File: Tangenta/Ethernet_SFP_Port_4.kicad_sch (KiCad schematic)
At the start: 17 parts, among them J25 HC-SFP-01L

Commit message: Fixes, before checks.
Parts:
- C166, C167, C168, C169: symbol C_Small:C_Small -> Device:C_Small
- J25: symbol HC-SFP-01L:HC-SFP-01L -> SFP_CAGE:HC-SFP-01L
- R141, R142, R143, R144, R145, R146, R147, R148, R149, R150, R151: symbol R_Small_US:R_Small_US -> Device:R_Small_US
- S1: symbol HC-SFP-20P:HC-SFP-20P -> SFP_Connector:HC-SFP-20P
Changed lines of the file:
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@@
 	)
 	(symbol
-		(lib_id "C_Small:C_Small")
+		(lib_id "Device:C_Small")
 		(at 66.04 64.77 270)
 		(unit 1)
@@
 	)
 	(symbol
-		(lib_id "R_Small_US:R_Small_US")
+		(lib_id "Device:R_Small_US")
 		(at 224.79 128.905 180)
 		(unit 1)
@@
 	)
 	(symbol
-		(lib_id "R_Small_US:R_Small_US")
+		(lib_id "Device:R_Small_US")
 		(at 139.7 118.11 90)
 		(unit 1)
@@
 	)
 	(symbol
-		(lib_id "HC-SFP-01L:HC-SFP-01L")
+		(lib_id "SFP_CAGE:HC-SFP-01L")
 		(at 159.385 76.835 0)
 		(unit 1)
@@
 	)
 	(symbol
-		(lib_id "R_Small_US:R_Small_US")
+		(lib_id "Device:R_Small_US")
 		(at 217.17 140.335 180)
 		(unit 1)
@@
 	)
 	(symbol
-		(lib_id "R_Small_US:R_Small_US")
+		(lib_id "Device:R_Small_US")
 		(at 139.7 133.35 90)
 		(unit 1)
@@
 	)
 	(symbol
-		(lib_id "C_Small:C_Small")
+		(lib_id "Device:C_Small")
 		(at 78.74 59.69 270)
 		(unit 1)
@@
 	)
 	(symbol
-		(lib_id "HC-SFP-20P:HC-SFP-20P")
+		(lib_id "SFP_Connector:HC-SFP-20P")
 		(at 159.385 127 0)
 		(unit 1)
@@
 	)
 	(symbol
-		(lib_id "R_Small_US:R_Small_US")
+		(lib_id "Device:R_Small_US")
 		(at 217.17 128.905 180)
 		(unit 1)
@@
 	)
 	(symbol
-		(lib_id "R_Small_US:R_Small_US")
+		(lib_id "Device:R_Small_US")
 		(at 198.755 113.03 180)
 		(unit 1)
@@
 	)
 	(symbol
-		(lib_id "C_Small:C_Small")
+		(lib_id "Device:C_Small")
 		(at 78.74 67.31 270)
 		(unit 1)
@@
 	)
 	(symbol
-		(lib_id "R_Small_US:R_Small_US")
+		(lib_id "Device:R_Small_US")
 		(at 224.79 140.335 180)
 		(unit 1)
@@
 	)
 	(symbol
-		(lib_id "C_Small:C_Small")
+		(lib_id "Device:C_Small")
 		(at 66.04 57.15 270)
 		(unit 1)
@@
 	)
 	(symbol
-		(lib_id "R_Small_US:R_Small_US")
+		(lib_id "Device:R_Small_US")
 		(at 198.755 125.095 180)
 		(unit 1)
@@
 	)
 	(symbol
-		(lib_id "R_Small_US:R_Small_US")
+		(lib_id "Device:R_Small_US")
 		(at 206.375 113.03 180)
 		(unit 1)
@@
 	)
 	(symbol
-		(lib_id "R_Small_US:R_Small_US")
+		(lib_id "Device:R_Small_US")
 		(at 139.7 128.27 90)
 		(unit 1)
@@
 	)
 	(symbol
-		(lib_id "R_Small_US:R_Small_US")
+		(lib_id "Device:R_Small_US")
 		(at 206.375 125.095 180)
 		(unit 1)

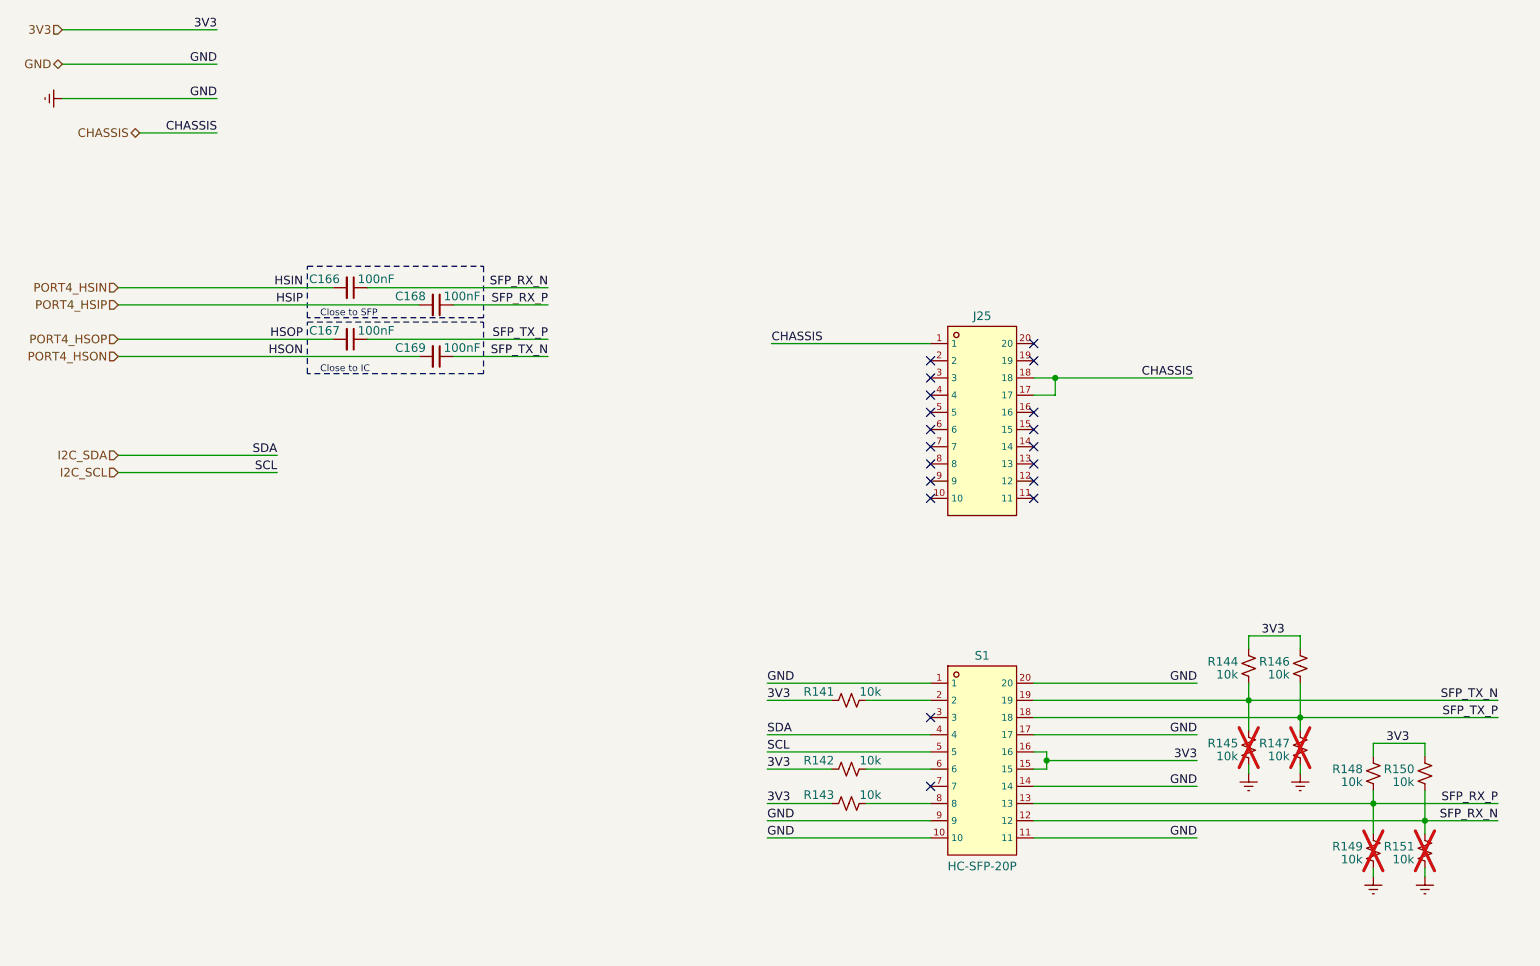
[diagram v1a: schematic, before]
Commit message: Reverting to the original design.
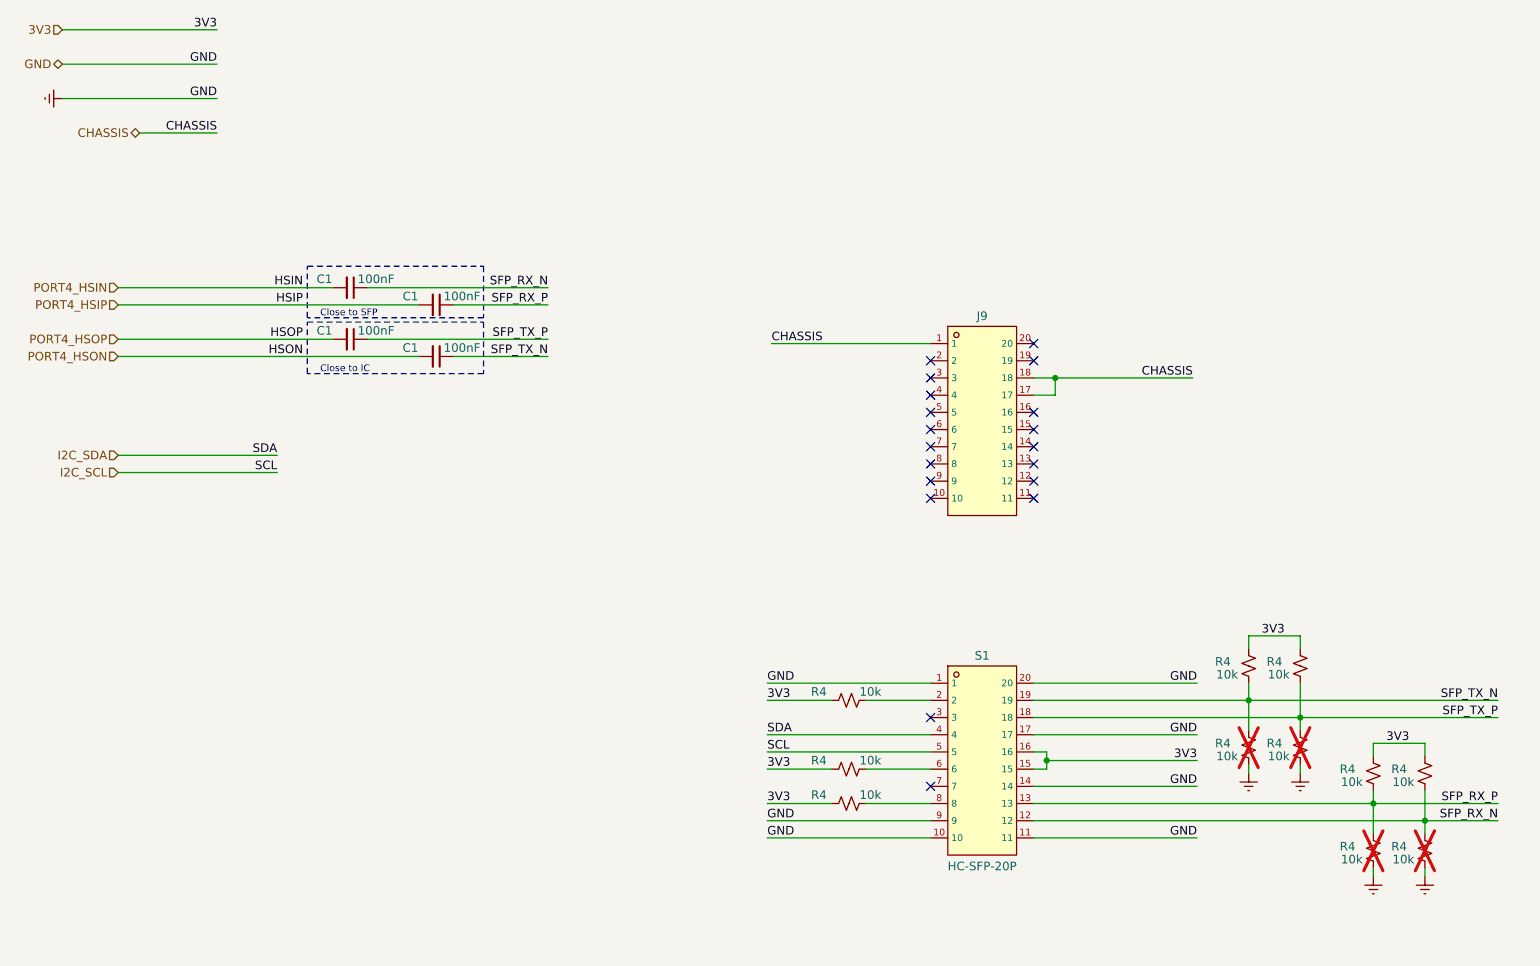
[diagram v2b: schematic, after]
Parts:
- C1: renamed from C167; symbol Device:C_Small -> CholaSymbolsPrjLib:C_Small
- C1: renamed from C168; symbol Device:C_Small -> CholaSymbolsPrjLib:C_Small
- C1: renamed from C169; symbol Device:C_Small -> CholaSymbolsPrjLib:C_Small
- C1: renamed from C166; symbol Device:C_Small -> CholaSymbolsPrjLib:C_Small
- J9: renamed from J25; symbol SFP_CAGE:HC-SFP-01L -> CholaSymbolsPrjLib:HC-SFP-01L
- R4: renamed from R150; symbol Device:R_Small_US -> CholaSymbolsPrjLib:R_Small_US
- R4: renamed from R141; symbol Device:R_Small_US -> CholaSymbolsPrjLib:R_Small_US
- R4: renamed from R149; symbol Device:R_Small_US -> CholaSymbolsPrjLib:R_Small_US
- R4: renamed from R143; symbol Device:R_Small_US -> CholaSymbolsPrjLib:R_Small_US
- R4: renamed from R148; symbol Device:R_Small_US -> CholaSymbolsPrjLib:R_Small_US
- R4: renamed from R144; symbol Device:R_Small_US -> CholaSymbolsPrjLib:R_Small_US
- R4: renamed from R151; symbol Device:R_Small_US -> CholaSymbolsPrjLib:R_Small_US
- R4: renamed from R145; symbol Device:R_Small_US -> CholaSymbolsPrjLib:R_Small_US
- R4: renamed from R146; symbol Device:R_Small_US -> CholaSymbolsPrjLib:R_Small_US
- R4: renamed from R142; symbol Device:R_Small_US -> CholaSymbolsPrjLib:R_Small_US
- R4: renamed from R147; symbol Device:R_Small_US -> CholaSymbolsPrjLib:R_Small_US
- S1: symbol SFP_Connector:HC-SFP-20P -> CholaSymbolsPrjLib:HC-SFP-20P

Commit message: initialize branch
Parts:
- renumbered C1 to C166, C1 to C167, C1 to C168, C1 to C169, J9 to J25, R4 to R141, R4 to R142, R4 to R143, R4 to R144, R4 to R145, R4 to R146, R4 to R147, R4 to R148, R4 to R149, R4 to R150, R4 to R151

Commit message: J6-J8,J22-J25,S1,U21
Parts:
- J25: footprint SFP_CAGE:TH_HC-SFP-01L -> CholaFootprintsPrjLib:TH_HC-SFP-01L
- S1: footprint SFP_Connector:SFP_Connector -> CholaFootprintsPrjLib:SFP_Connector
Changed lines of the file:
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@@
       (effects (font (size 1.27 1.27)) hide)
     )
-    (property "Footprint" "SFP_CAGE:TH_HC-SFP-01L" (at 159.385 86.995 0)
+    (property "Footprint" "CholaFootprintsPrjLib:TH_HC-SFP-01L" (at 159.385 86.995 0)
       (effects (font (size 1.27 1.27) italic) hide)
     )
@@
       (effects (font (size 1.27 1.27)))
     )
-    (property "Footprint" "SFP_Connector:SFP_Connector" (at 159.385 137.16 0)
+    (property "Footprint" "CholaFootprintsPrjLib:SFP_Connector" (at 159.385 137.16 0)
       (effects (font (size 1.27 1.27) italic) hide)
     )

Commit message: Removing component association with previous project (local) libraries.
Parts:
- C166, C167, C168, C169: symbol CholaSymbolsPrjLib:C_Small -> C_Small:C_Small
- J25: footprint CholaFootprintsPrjLib:TH_HC-SFP-01L -> TH_HC-SFP-01L:TH_HC-SFP-01L; symbol CholaSymbolsPrjLib:HC-SFP-01L -> HC-SFP-01L:HC-SFP-01L
- R141, R142, R143, R144, R145, R146, R147, R148, R149, R150, R151: symbol CholaSymbolsPrjLib:R_Small_US -> R_Small_US:R_Small_US
- S1: footprint CholaFootprintsPrjLib:SFP_Connector -> SFP_Connector:SFP_Connector; symbol CholaSymbolsPrjLib:HC-SFP-20P -> HC-SFP-20P:HC-SFP-20P
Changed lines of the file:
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@@
 	)
 	(symbol
-		(lib_id "CholaSymbolsPrjLib:C_Small")
+		(lib_id "C_Small:C_Small")
 		(at 66.04 64.77 270)
 		(unit 1)
@@
 	)
 	(symbol
-		(lib_id "CholaSymbolsPrjLib:R_Small_US")
+		(lib_id "R_Small_US:R_Small_US")
 		(at 224.79 128.905 180)
 		(unit 1)
@@
 	)
 	(symbol
-		(lib_id "CholaSymbolsPrjLib:R_Small_US")
+		(lib_id "R_Small_US:R_Small_US")
 		(at 139.7 118.11 90)
 		(unit 1)
@@
 	)
 	(symbol
-		(lib_id "CholaSymbolsPrjLib:HC-SFP-01L")
+		(lib_id "HC-SFP-01L:HC-SFP-01L")
 		(at 159.385 76.835 0)
 		(unit 1)
@@
 			)
 		)
-		(property "Footprint" "CholaFootprintsPrjLib:TH_HC-SFP-01L"
+		(property "Footprint" "TH_HC-SFP-01L:TH_HC-SFP-01L"
 			(at 159.385 86.995 0)
 			(effects
@@
 	)
 	(symbol
-		(lib_id "CholaSymbolsPrjLib:R_Small_US")
+		(lib_id "R_Small_US:R_Small_US")
 		(at 217.17 140.335 180)
 		(unit 1)
@@
 	)
 	(symbol
-		(lib_id "CholaSymbolsPrjLib:R_Small_US")
+		(lib_id "R_Small_US:R_Small_US")
 		(at 139.7 133.35 90)
 		(unit 1)
@@
 	)
 	(symbol
-		(lib_id "CholaSymbolsPrjLib:C_Small")
+		(lib_id "C_Small:C_Small")
 		(at 78.74 59.69 270)
 		(unit 1)
@@
 	)
 	(symbol
-		(lib_id "CholaSymbolsPrjLib:HC-SFP-20P")
+		(lib_id "HC-SFP-20P:HC-SFP-20P")
 		(at 159.385 127 0)
 		(unit 1)
@@
 			)
 		)
-		(property "Footprint" "CholaFootprintsPrjLib:SFP_Connector"
+		(property "Footprint" "SFP_Connector:SFP_Connector"
 			(at 159.385 137.16 0)
 			(effects
@@
 	)
 	(symbol
-		(lib_id "CholaSymbolsPrjLib:R_Small_US")
+		(lib_id "R_Small_US:R_Small_US")
 		(at 217.17 128.905 180)
 		(unit 1)
@@
 	)
 	(symbol
-		(lib_id "CholaSymbolsPrjLib:R_Small_US")
+		(lib_id "R_Small_US:R_Small_US")
 		(at 198.755 113.03 180)
 		(unit 1)
@@
 	)
 	(symbol
-		(lib_id "CholaSymbolsPrjLib:C_Small")
+		(lib_id "C_Small:C_Small")
 		(at 78.74 67.31 270)
 		(unit 1)
@@
 	)
 	(symbol
-		(lib_id "CholaSymbolsPrjLib:R_Small_US")
+		(lib_id "R_Small_US:R_Small_US")
 		(at 224.79 140.335 180)
 		(unit 1)
@@
 	)
 	(symbol
-		(lib_id "CholaSymbolsPrjLib:C_Small")
+		(lib_id "C_Small:C_Small")
 		(at 66.04 57.15 270)
 		(unit 1)
@@
 	)
 	(symbol
-		(lib_id "CholaSymbolsPrjLib:R_Small_US")
+		(lib_id "R_Small_US:R_Small_US")
 		(at 198.755 125.095 180)
 		(unit 1)
@@
 	)
 	(symbol
-		(lib_id "CholaSymbolsPrjLib:R_Small_US")
+		(lib_id "R_Small_US:R_Small_US")
 		(at 206.375 113.03 180)
 		(unit 1)
@@
 	)
 	(symbol
-		(lib_id "CholaSymbolsPrjLib:R_Small_US")
+		(lib_id "R_Small_US:R_Small_US")
 		(at 139.7 128.27 90)
 		(unit 1)
@@
 	)
 	(symbol
-		(lib_id "CholaSymbolsPrjLib:R_Small_US")
+		(lib_id "R_Small_US:R_Small_US")
 		(at 206.375 125.095 180)
 		(unit 1)

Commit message: Fixes, continued...
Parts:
- C166, C167, C168, C169: symbol C_Small:C_Small -> Device:C_Small
- R141, R142, R143, R144, R145, R146, R147, R148, R149, R150, R151: symbol R_Small_US:R_Small_US -> Device:R_Small_US
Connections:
- net 3V3: no longer R141.1, R142.1, R143.1, R144.2, R146.2, R148.2, R150.2
- net GNDREF: no longer R145.1, R147.1, R149.1, R151.1
- net PORT4_HSIN: no longer C166.2
- net PORT4_HSIP: no longer C168.2
- net PORT4_HSON: no longer C169.2
- net PORT4_HSOP: no longer C167.2
- net SFP_RX_N: no longer C166.1, R150.1, R151.2
- net SFP_RX_P: no longer C168.1, R148.1, R149.2
- net SFP_TX_N: no longer C169.1, R144.1, R145.2
- net SFP_TX_P: no longer C167.1, R146.1, R147.2
- net at S1.2: no longer R141.2
- net at S1.8: no longer R143.2
- net at S1.6: no longer R142.2
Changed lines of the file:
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@@
 	)
 	(symbol
-		(lib_id "C_Small:C_Small")
+		(lib_id "Device:C_Small")
 		(at 66.04 64.77 270)
 		(unit 1)
@@
 	)
 	(symbol
-		(lib_id "R_Small_US:R_Small_US")
+		(lib_id "Device:R_Small_US")
 		(at 224.79 128.905 180)
 		(unit 1)
@@
 	)
 	(symbol
-		(lib_id "R_Small_US:R_Small_US")
+		(lib_id "Device:R_Small_US")
 		(at 139.7 118.11 90)
 		(unit 1)
@@
 	)
 	(symbol
-		(lib_id "R_Small_US:R_Small_US")
+		(lib_id "Device:R_Small_US")
 		(at 217.17 140.335 180)
 		(unit 1)
@@
 	)
 	(symbol
-		(lib_id "R_Small_US:R_Small_US")
+		(lib_id "Device:R_Small_US")
 		(at 139.7 133.35 90)
 		(unit 1)
@@
 	)
 	(symbol
-		(lib_id "C_Small:C_Small")
+		(lib_id "Device:C_Small")
 		(at 78.74 59.69 270)
 		(unit 1)
@@
 	)
 	(symbol
-		(lib_id "R_Small_US:R_Small_US")
+		(lib_id "Device:R_Small_US")
 		(at 217.17 128.905 180)
 		(unit 1)
@@
 	)
 	(symbol
-		(lib_id "R_Small_US:R_Small_US")
+		(lib_id "Device:R_Small_US")
 		(at 198.755 113.03 180)
 		(unit 1)
@@
 	)
 	(symbol
-		(lib_id "C_Small:C_Small")
+		(lib_id "Device:C_Small")
 		(at 78.74 67.31 270)
 		(unit 1)
@@
 	)
 	(symbol
-		(lib_id "R_Small_US:R_Small_US")
+		(lib_id "Device:R_Small_US")
 		(at 224.79 140.335 180)
 		(unit 1)
@@
 	)
 	(symbol
-		(lib_id "C_Small:C_Small")
+		(lib_id "Device:C_Small")
 		(at 66.04 57.15 270)
 		(unit 1)
@@
 	)
 	(symbol
-		(lib_id "R_Small_US:R_Small_US")
+		(lib_id "Device:R_Small_US")
 		(at 198.755 125.095 180)
 		(unit 1)
@@
 	)
 	(symbol
-		(lib_id "R_Small_US:R_Small_US")
+		(lib_id "Device:R_Small_US")
 		(at 206.375 113.03 180)
 		(unit 1)
@@
 	)
 	(symbol
-		(lib_id "R_Small_US:R_Small_US")
+		(lib_id "Device:R_Small_US")
 		(at 139.7 128.27 90)
 		(unit 1)
@@
 	)
 	(symbol
-		(lib_id "R_Small_US:R_Small_US")
+		(lib_id "Device:R_Small_US")
 		(at 206.375 125.095 180)
 		(unit 1)

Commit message: Fixes, continued...
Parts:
- C166, C167, C168, C169: symbol Device:C_Small -> C_Small:C_Small
- J25: footprint TH_HC-SFP-01L:TH_HC-SFP-01L -> SFP_CAGE:TH_HC-SFP-01L
- R141, R142, R143, R144, R145, R146, R147, R148, R149, R150, R151: symbol Device:R_Small_US -> R_Small_US:R_Small_US
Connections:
- net 3V3: now also R141.1, R142.1, R143.1, R144.2, R146.2, R148.2, R150.2
- net GNDREF: now also R145.1, R147.1, R149.1, R151.1
- net PORT4_HSIN: now also C166.2
- net PORT4_HSIP: now also C168.2
- net PORT4_HSON: now also C169.2
- net PORT4_HSOP: now also C167.2
- net SFP_RX_N: now also C166.1, R150.1, R151.2
- net SFP_RX_P: now also C168.1, R148.1, R149.2
- net SFP_TX_N: now also C169.1, R144.1, R145.2
- net SFP_TX_P: now also C167.1, R146.1, R147.2
- net at S1.2: now also R141.2
- net at S1.6: now also R142.2
- net at S1.8: now also R143.2
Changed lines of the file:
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@@
 	)
 	(symbol
-		(lib_id "Device:C_Small")
+		(lib_id "C_Small:C_Small")
 		(at 66.04 64.77 270)
 		(unit 1)
@@
 	)
 	(symbol
-		(lib_id "Device:R_Small_US")
+		(lib_id "R_Small_US:R_Small_US")
 		(at 224.79 128.905 180)
 		(unit 1)
@@
 	)
 	(symbol
-		(lib_id "Device:R_Small_US")
+		(lib_id "R_Small_US:R_Small_US")
 		(at 139.7 118.11 90)
 		(unit 1)
@@
 			)
 		)
-		(property "Footprint" "TH_HC-SFP-01L:TH_HC-SFP-01L"
+		(property "Footprint" "SFP_CAGE:TH_HC-SFP-01L"
 			(at 159.385 86.995 0)
 			(effects
@@
 	)
 	(symbol
-		(lib_id "Device:R_Small_US")
+		(lib_id "R_Small_US:R_Small_US")
 		(at 217.17 140.335 180)
 		(unit 1)
@@
 	)
 	(symbol
-		(lib_id "Device:R_Small_US")
+		(lib_id "R_Small_US:R_Small_US")
 		(at 139.7 133.35 90)
 		(unit 1)
@@
 	)
 	(symbol
-		(lib_id "Device:C_Small")
+		(lib_id "C_Small:C_Small")
 		(at 78.74 59.69 270)
 		(unit 1)
@@
 	)
 	(symbol
-		(lib_id "Device:R_Small_US")
+		(lib_id "R_Small_US:R_Small_US")
 		(at 217.17 128.905 180)
 		(unit 1)
@@
 	)
 	(symbol
-		(lib_id "Device:R_Small_US")
+		(lib_id "R_Small_US:R_Small_US")
 		(at 198.755 113.03 180)
 		(unit 1)
@@
 	)
 	(symbol
-		(lib_id "Device:C_Small")
+		(lib_id "C_Small:C_Small")
 		(at 78.74 67.31 270)
 		(unit 1)
@@
 	)
 	(symbol
-		(lib_id "Device:R_Small_US")
+		(lib_id "R_Small_US:R_Small_US")
 		(at 224.79 140.335 180)
 		(unit 1)
@@
 	)
 	(symbol
-		(lib_id "Device:C_Small")
+		(lib_id "C_Small:C_Small")
 		(at 66.04 57.15 270)
 		(unit 1)
@@
 	)
 	(symbol
-		(lib_id "Device:R_Small_US")
+		(lib_id "R_Small_US:R_Small_US")
 		(at 198.755 125.095 180)
 		(unit 1)
@@
 	)
 	(symbol
-		(lib_id "Device:R_Small_US")
+		(lib_id "R_Small_US:R_Small_US")
 		(at 206.375 113.03 180)
 		(unit 1)
@@
 	)
 	(symbol
-		(lib_id "Device:R_Small_US")
+		(lib_id "R_Small_US:R_Small_US")
 		(at 139.7 128.27 90)
 		(unit 1)
@@
 	)
 	(symbol
-		(lib_id "Device:R_Small_US")
+		(lib_id "R_Small_US:R_Small_US")
 		(at 206.375 125.095 180)
 		(unit 1)
